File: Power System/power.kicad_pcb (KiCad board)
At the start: 2 copper layers, 139.7 x 100.3 mm, 44 parts, among them J1 PC104_40Pin_2.54mm, J2 Charge Cable, J3 Battery Pack, J4 IDC Header, U1 ds2781e+, U2 LT3461AES6-TRPBF

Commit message: Swapped LT3461a for LT3461 and changed pins on connector
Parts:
- U2: value LT3461AES6-TRPBF -> LT3461ES6-TRMPBF; footprint LT3461AES6-TRPBF:LT3461AES6-TRPBF -> LT3461ES6_TRMPBF:LT3461ES6-TRMPBF
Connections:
- net /AUDIO_ALERT renamed /SIPM_1_Analog_Voltage
- net /IRIDIUM_NET_AVAIL renamed /SIPM_1_RESET
- net /IRIDIUM_PWR_CTRL renamed /SIPM_2_Analog_Voltage
- net /IRIDIUM_RX renamed /OTHER_RX
- net /IRIDIUM_TX renamed /OTHER_TX
- net /POD_WAKE renamed /Battery_Voltage
- net /RADIO_WAKE renamed /SIPM_2_RESET
- J1 pad 21: +3V3 -> /SIPM_Power

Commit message: Changed POD_TX and POD_RX to SERIAL_RX and SERIAL_TX
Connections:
- net /POD_RX renamed /SERIAL_RX
- net /POD_TX renamed /SERIAL_TX

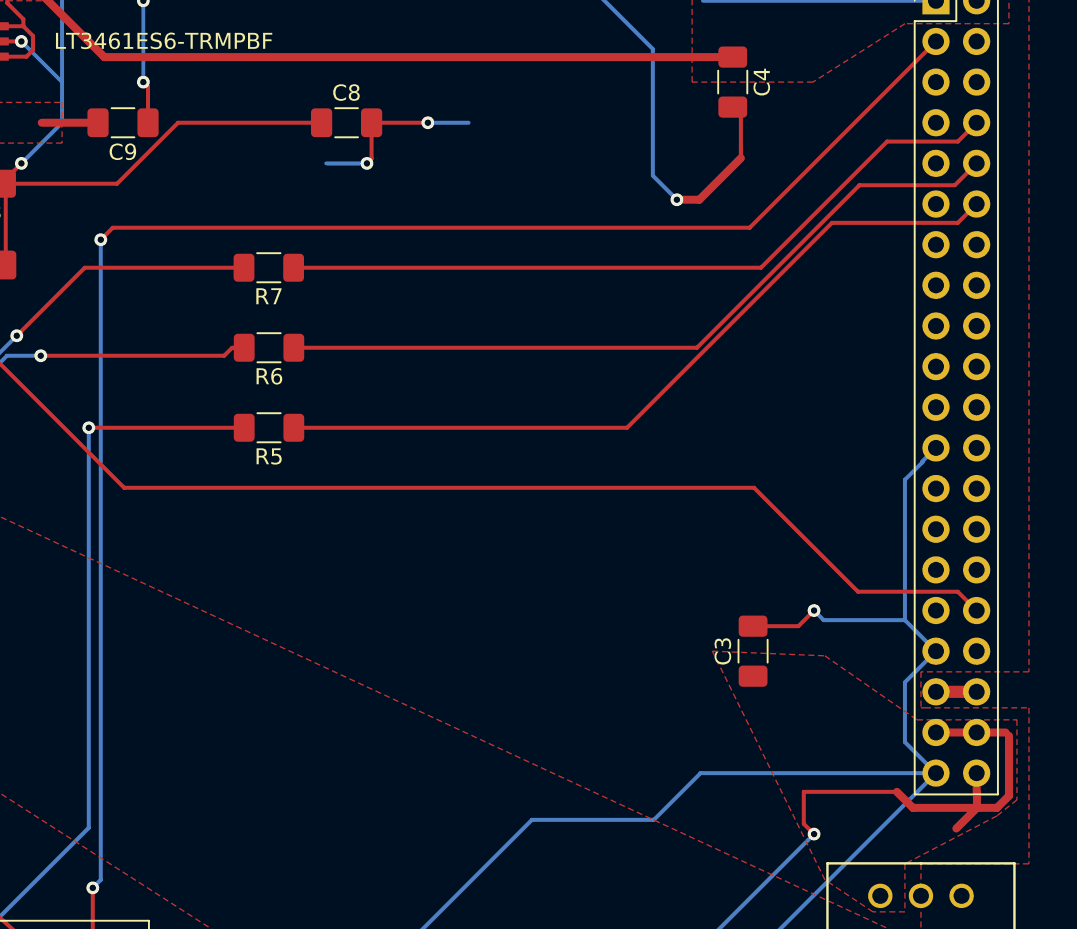
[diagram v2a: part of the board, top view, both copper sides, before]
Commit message: Routed SIPM_Power and renamed Battery Voltage to unclaimed
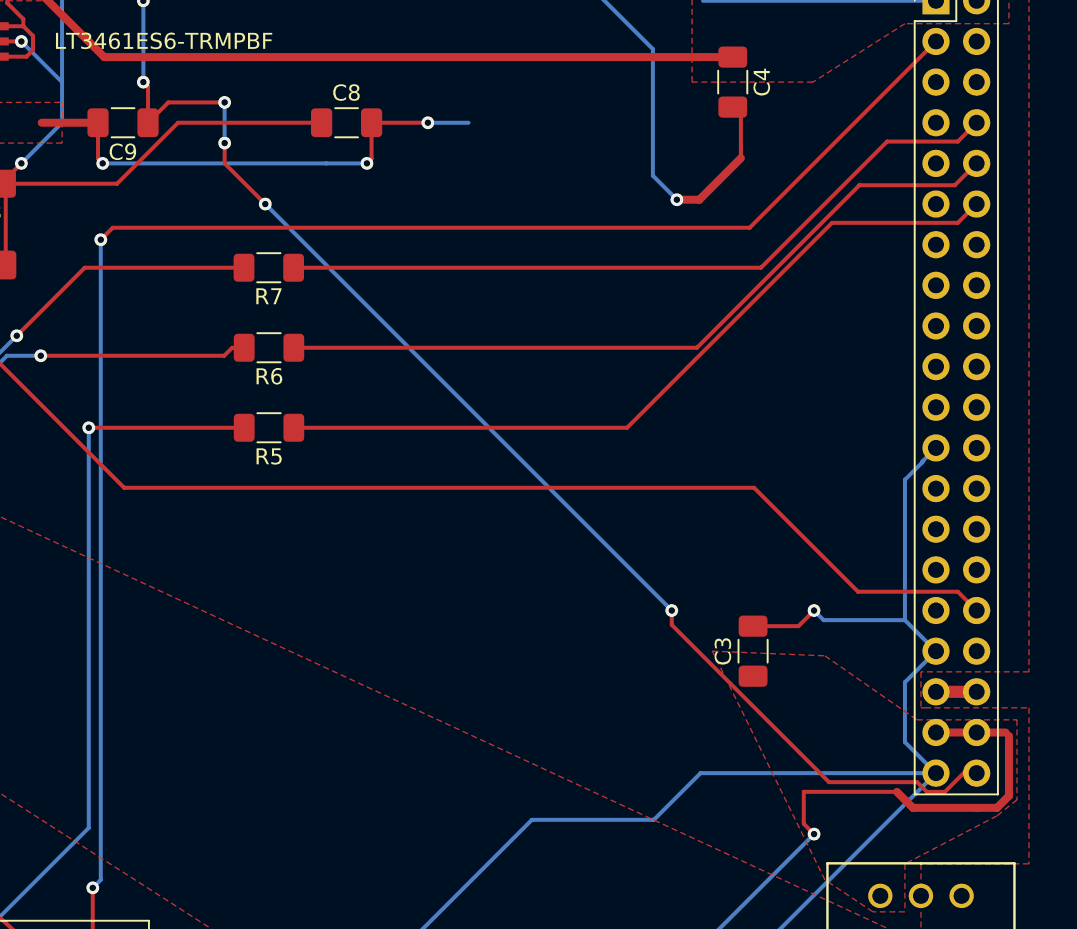
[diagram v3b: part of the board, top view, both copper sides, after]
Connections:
- net /Battery_Voltage renamed /Unclaimed
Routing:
- net /SIPM_Power: track 11.3 -> 84.5 mm, vias 2 -> 6
- net GND: track 413.7 -> 430.3 mm, vias 10 -> 11
- net +3V3: track 147.6 -> 143.6 mm

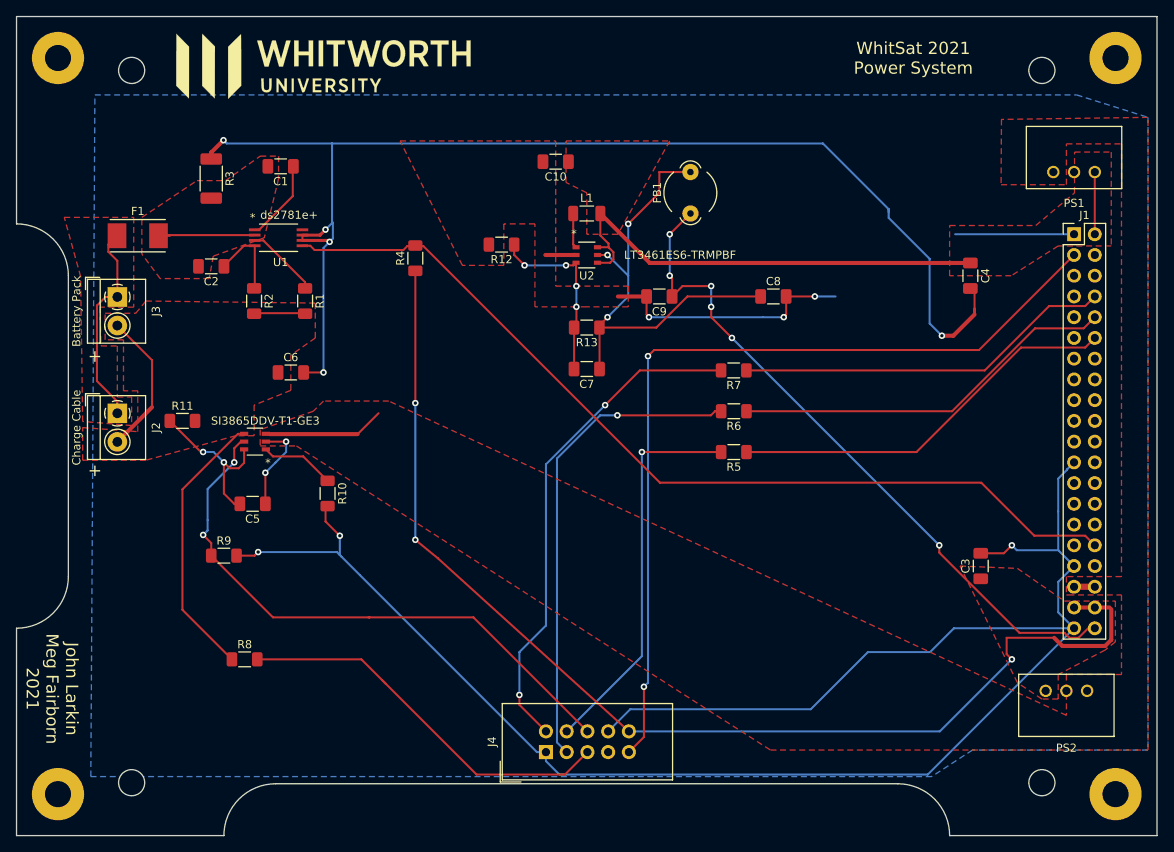
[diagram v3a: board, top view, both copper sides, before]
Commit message: Switched some footprints and created gerber files
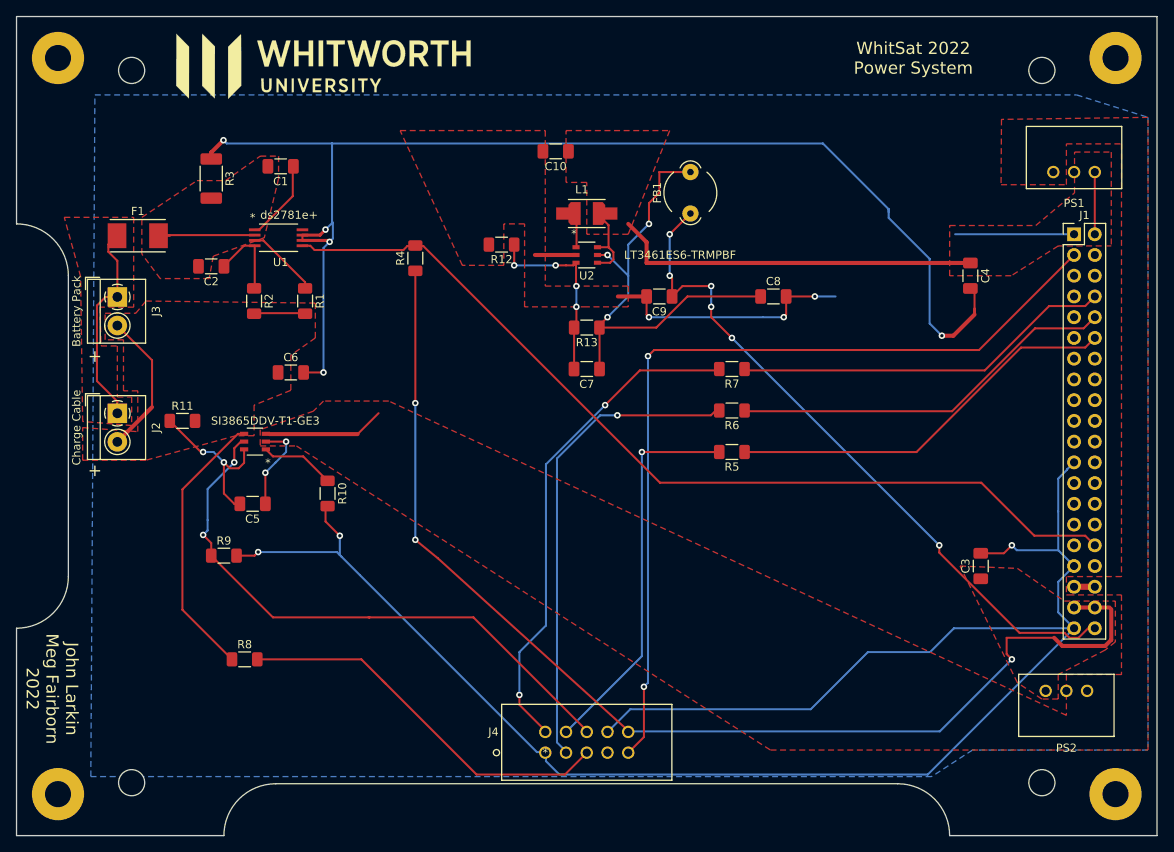
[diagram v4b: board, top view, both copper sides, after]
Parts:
- J4: value IDC Header -> 302-S101; footprint Connector_IDC:IDC-Header_2x05_P2.54mm_Vertical -> 302-S101Connector:302-S101
- L1: footprint Inductor_SMD:L_1206_3216Metric_Pad1.22x1.90mm_HandSolder -> LQH43NH470J03L-Inductor:IND_LQH43NH470J03L
- moved C10 1.27 mm to (91.4, 41.9)
- moved R7 0.28 mm to (113.0, 68.6)
- moved R6 0.25 mm to (113.0, 73.7)
- moved R5 0.23 mm to (113.0, 78.7)
- moved J4 0.11 mm to (90.2, 115.6), turned to 0 degrees
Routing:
- net +5V: track 65.2 -> 63.0 mm
- net GND: track 430.3 -> 431.6 mm
- net Net-(C7-Pad2): track 22.7 -> 23.4 mm
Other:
- board text added: "John Larkin Meg Fairborn 2022"
- board text added: "WhitSat 2022 Power System"
- board text removed: "John Larkin Meg Fairborn 2021"
- board text removed: "WhitSat 2021 Power System"

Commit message: Fingers Crossed This Doesn't Mess Stuff Up
GitHub lost track of the repository on my computers, and I messed a bunch of stuff up trying to fix the issue, but I think it is fixed now... I also added the old connector for the switch Dr. Larkin used on his power board so hopefully that change is also committed...
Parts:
- C9: value 1uF -> 10uF
- FB1: value 2.5k Ferrite Bead -> 2.7k Ferrite Bead; footprint Ferrite_THT:LairdTech_28C0236-0JW-10 -> 742792095:BEADC2012X110N
- J4: value 302-S101 -> IDC Header; footprint 302-S101Connector:302-S101 -> Connector_IDC:IDC-Header_2x05_P2.54mm_Vertical
- R12: value 10k -> 11k
- R5: value 3.4 -> 220
- R6: value 5.1 -> 220
- R7: value 66.5 -> 220
- moved J4 1.80 mm to (88.9, 114.3), turned to 90 degrees
- moved L1 1.27 mm to (95.2, 48.3)
- moved FB1 1.27 mm to (108.0, 48.3)
- moved R5 1.27 mm to (114.3, 78.7)
- moved R7 1.27 mm to (111.8, 68.6)
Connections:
- J4 pad 7: Net-(J4-Pad7) -> unconnected-(J4-Pad7)
- U1 pad 8: Net-(U1-Pad8) -> unconnected-(U1-Pad8)
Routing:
- net Net-(R7-Pad2): track 61.7 -> 58.4 mm
- net Net-(C7-Pad1): track 57.1 -> 54.4 mm
- net /PWR_ENABLE: track 71.9 -> 70.1 mm
- net GND: track 431.6 -> 433.3 mm
- net /LED_A: track 46.5 -> 48.0 mm
- net +5V: track 63.0 -> 64.3 mm
- net /LED_C: track 48.5 -> 47.4 mm
- net Net-(R6-Pad2): track 59.4 -> 58.4 mm
- net /EXT_TEMP: track 106.8 -> 107.6 mm
- net Net-(R8-Pad2): track 48.0 -> 48.6 mm
- net Net-(R5-Pad2): track 47.8 -> 48.4 mm
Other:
- outline, holes or cut-outs redrawn
- net class Default removed
